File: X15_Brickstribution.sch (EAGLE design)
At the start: 42 parts, among them Q1 310mA/60V/1.6Ω

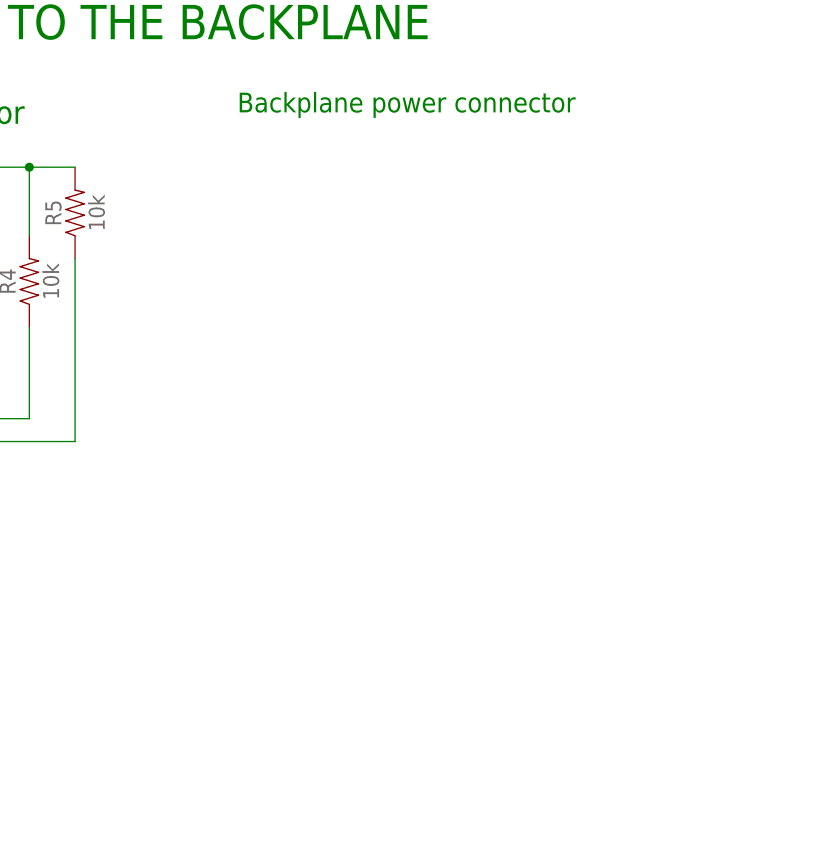
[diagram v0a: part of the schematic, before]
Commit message: Schematic V1 - Added Backplane Connections
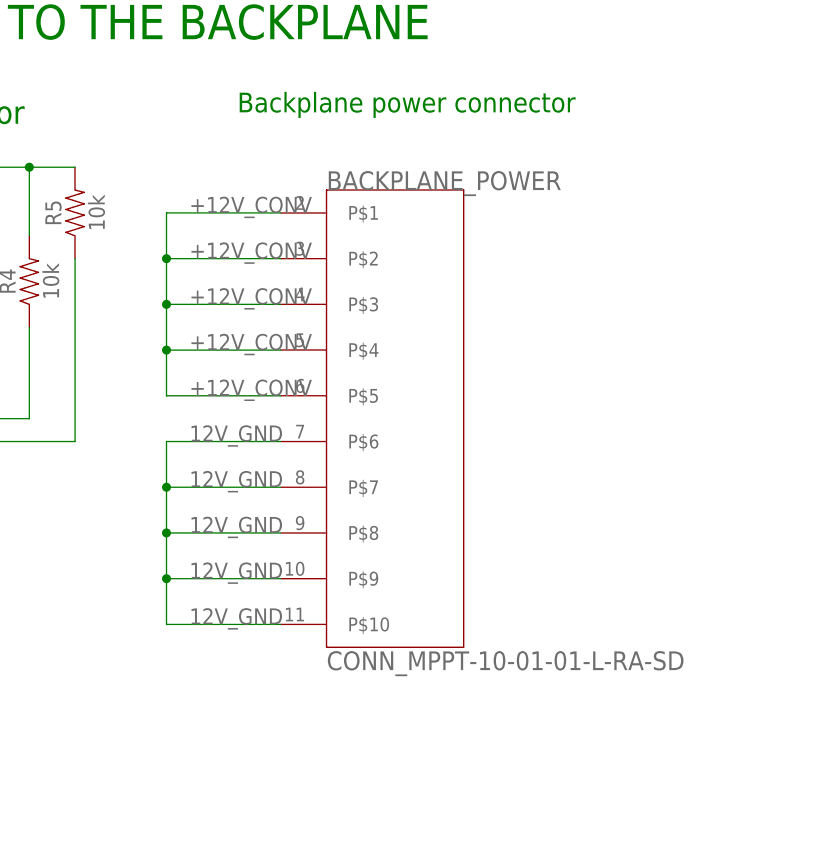
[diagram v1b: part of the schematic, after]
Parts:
- added BACKPLANE_POWER: CONN_MPPT-10-01-01-L-RA-SD, X15_Brickstribution:CONN_MPPT-10-01-01-L-RA-SD
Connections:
- net +12V_CONV: now also BACKPLANE_POWER.P$1, BACKPLANE_POWER.P$2, BACKPLANE_POWER.P$3, BACKPLANE_POWER.P$4, BACKPLANE_POWER.P$5
- net 12V_GND: now also BACKPLANE_POWER.P$10, BACKPLANE_POWER.P$6, BACKPLANE_POWER.P$7, BACKPLANE_POWER.P$8, BACKPLANE_POWER.P$9
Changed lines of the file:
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@@
 <part name="D10" library="SparkFun-LED" library_urn="urn:adsk.eagle:library:529" deviceset="LED-BLUE" device="0603" package3d_urn="urn:adsk.eagle:package:39354/1" value="BLUE"/>
 <part name="D11" library="SparkFun-LED" library_urn="urn:adsk.eagle:library:529" deviceset="LED-WHITE" device="0603" package3d_urn="urn:adsk.eagle:package:39354/1" value="WHITE"/>
+<part name="BACKPLANE_POWER" library="X15_Brickstribution" deviceset="CONN_MPPT-10-01-01-L-RA-SD" device=""/>
 </parts>
 <sheets>
@@
 <attribute name="VALUE" x="334.772" y="78.105" size="1.778" layer="96" font="vector" rot="R180" align="top-left"/>
 </instance>
+<instance part="BACKPLANE_POWER" gate="A" x="355.6" y="180.34" smashed="yes">
+<attribute name="NAME" x="347.98" y="205.74" size="2.0828" layer="95" ratio="6"/>
+<attribute name="VALUE" x="347.98" y="152.4" size="2.0828" layer="95" ratio="6"/>
+</instance>
 </instances>
 <busses>
@@
 <label x="345.44" y="101.6" size="1.778" layer="95" align="bottom-right"/>
 </segment>
+<segment>
+<pinref part="BACKPLANE_POWER" gate="A" pin="P$6"/>
+<wire x1="342.9" y1="177.8" x2="330.2" y2="177.8" width="0.1524" layer="91"/>
+<label x="332.74" y="177.8" size="1.778" layer="95"/>
+<wire x1="330.2" y1="177.8" x2="330.2" y2="172.72" width="0.1524" layer="91"/>
+<pinref part="BACKPLANE_POWER" gate="A" pin="P$8"/>
+<wire x1="330.2" y1="172.72" x2="330.2" y2="167.64" width="0.1524" layer="91"/>
+<wire x1="342.9" y1="167.64" x2="330.2" y2="167.64" width="0.1524" layer="91"/>
+<label x="332.74" y="167.64" size="1.778" layer="95"/>
+<pinref part="BACKPLANE_POWER" gate="A" pin="P$7"/>
+<wire x1="342.9" y1="172.72" x2="330.2" y2="172.72" width="0.1524" layer="91"/>
+<label x="332.74" y="172.72" size="1.778" layer="95"/>
+<junction x="330.2" y="172.72"/>
+<pinref part="BACKPLANE_POWER" gate="A" pin="P$9"/>
+<wire x1="342.9" y1="162.56" x2="330.2" y2="162.56" width="0.1524" layer="91"/>
+<label x="332.74" y="162.56" size="1.778" layer="95"/>
+<wire x1="330.2" y1="167.64" x2="330.2" y2="162.56" width="0.1524" layer="91"/>
+<junction x="330.2" y="167.64"/>
+<pinref part="BACKPLANE_POWER" gate="A" pin="P$10"/>
+<wire x1="342.9" y1="157.48" x2="330.2" y2="157.48" width="0.1524" layer="91"/>
+<label x="332.74" y="157.48" size="1.778" layer="95"/>
+<wire x1="330.2" y1="162.56" x2="330.2" y2="157.48" width="0.1524" layer="91"/>
+<junction x="330.2" y="162.56"/>
+</segment>
 </net>
 <net name="+12V" class="0">
@@
 <wire x1="25.4" y1="121.92" x2="25.4" y2="119.38" width="0.1524" layer="91"/>
 </segment>
-</net>
+<segment>
+<pinref part="BACKPLANE_POWER" gate="A" pin="P$1"/>
+<wire x1="342.9" y1="203.2" x2="330.2" y2="203.2" width="0.1524" layer="91"/>
+<label x="332.74" y="203.2" size="1.778" layer="95"/>
+<pinref part="BACKPLANE_POWER" gate="A" pin="P$2"/>
+<wire x1="342.9" y1="198.12" x2="330.2" y2="198.12" width="0.1524" layer="91"/>
+<label x="332.74" y="198.12" size="1.778" layer="95"/>
+<wire x1="330.2" y1="203.2" x2="330.2" y2="198.12" width="0.1524" layer="91"/>
+<pinref part="BACKPLANE_POWER" gate="A" pin="P$3"/>
+<wire x1="342.9" y1="193.04" x2="330.2" y2="193.04" width="0.1524" layer="91"/>
+<label x="332.74" y="193.04" size="1.778" layer="95"/>
+<wire x1="330.2" y1="198.12" x2="330.2" y2="193.04" width="0.1524" layer="91"/>
+<junction x="330.2" y="198.12"/>
+<pinref part="BACKPLANE_POWER" gate="A" pin="P$4"/>
+<wire x1="342.9" y1="187.96" x2="330.2" y2="187.96" width="0.1524" layer="91"/>
+<label x="332.74" y="187.96" size="1.778" layer="95"/>
+<wire x1="330.2" y1="193.04" x2="330.2" y2="187.96" width="0.1524" layer="91"/>
+<junction x="330.2" y="193.04"/>
+<pinref part="BACKPLANE_POWER" gate="A" pin="P$5"/>
+<wire x1="342.9" y1="182.88" x2="330.2" y2="182.88" width="0.1524" layer="91"/>
+<label x="332.74" y="182.88" size="1.778" layer="95"/>
+<wire x1="330.2" y1="187.96" x2="330.2" y2="182.88" width="0.1524" layer="91"/>
+<junction x="330.2" y="187.96"/>
+</segment>
+</net>

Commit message: Schematic Revision V1
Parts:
- added C10, C17, C18, C19, C8, C9: 2.2uF, SparkFun-Capacitors:2.2UF-0603-10V-20%
- added C11, C20: 1000uF, X15_Brickstribution:CAP_PCG1A102MCL1GSCAP_PC_10X12P7_NCH-M
- added C12, C21: 1.0uF, SparkFun-Capacitors:1.0UF-0603-16V-10%
- added C13, C4: 0.22uF, SparkFun-Capacitors:0.22UF-0603-25V-10%
- added C14, C5: 2.2nF, SparkFun-Capacitors:2.2NF/2200PF-0603-50V-10%
- added C15, C6: 390pF, SparkFun-Capacitors:390NF-0603-10V-10%
- added C16, C7: 22nF, SparkFun-Capacitors:22NF/22,000PF-0603-50V-10%
- added R12, R16: 15k, SparkFun-Resistors:15KOHM-0603-1/10W-1%
- added R13, R17: 16k, SparkFun-Resistors:16.2KOHM-0603-1/10W-1%
- added R14, R18: 10k, SparkFun-Resistors:10KOHM-0603-1/10W-1%
- added R15, R19: 20k, SparkFun-Resistors:20KOHM-0603-1/10W-1%
- added R20: DIODE_RBQ30NS45AFHTLTRANS_R5009FNJ_ROM-M, X15_Brickstribution:DIODE_RBQ30NS45AFHTLTRANS_R5009FNJ_ROM-M
- added U$2, U$3: 40uH, X15_Brickstribution:IND_PG1096_26X26_PUL-M
- added U$4: CONN_MPPT-10-01-01-L-RA-SD, X15_Brickstribution:CONN_MPPT-10-01-01-L-RA-SD
- added U1, U2: IC_L4970A, X15_Brickstribution:IC_L4970A
- added U3, U4: DIODE_STPS1545CT, X15_Brickstribution:DIODE_STPS1545CT
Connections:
- new net +7.4V_SERVO: R20.2, U$4.P$1, U$4.P$2, U$4.P$3, U$4.P$4, U$4.P$5
- new net N$11: C7.1, R12.2
- new net N$14: C13.1, C4.1, U1.BOOT, U2.BOOT
- new net N$15: C14.2, C5.2, U1.C_OSC, U2.C_OSC
- new net N$16: C15.2, C16.2, C6.2, C7.2, U1.FCOMP, U2.FCOMP
- new net N$17: R13.2, R17.2, U1.R_OSC, U2.R_OSC
- new net N$18: C17.2, C8.2, U1.SS, U2.SS
- new net N$20: C18.2, C9.2, U1.VREF, U2.VREF
- new net N$22: C13.2, C4.2, U$2.2, U$3.2, U1.OUT, U2.OUT, U3.2, U4.2
- new net N$24: C10.2, C19.2, U1.VSTART, U2.VSTART
- new net N$3: C16.1, R16.2
- new net NC: U1.RST_DLY, U1.RST_OUT, U1.SYNC, U2.RST_DLY, U2.RST_OUT, U2.SYNC
- new net VOUT1: C11.1, C12.2, R14.2, R20.3, U$2.1
- new net VOUT2: C20.1, C21.2, R18.2, R20.1, U$3.1
- new net VREF1: R14.1, R15.2, U1.FB
- new net VREF2: R18.1, R19.2, U2.FB
- net +12V_CONV: now also U1.VI, U2.VI
- net 12V_GND: now also C10.1, C11.2, C12.1, C14.1, C15.1, C17.1, C18.1, C19.1, C20.2, C21.1, C5.1, C6.1, C8.1, C9.1, R12.1, R13.1, R15.1, R16.1, R17.1, R19.1, U$4.P$10, U$4.P$6, U$4.P$7, U$4.P$8, U$4.P$9, U1.GND, U1.RST, U2.GND, U2.RST, U3.1, U3.3, U4.1, U4.3
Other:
- note added: "CONNECTIONS TO SERVOS"

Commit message: Cleaned all backup files and updated schematic for revisions v1
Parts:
- removed BRICK: BMR480_CONNECTOR, X15_Brickstribution:BMR480_CONNECTOR
- removed C10, C17, C18, C19, C8, C9: 2.2uF, SparkFun-Capacitors:2.2UF-0603-10V-20%
- removed C11, C20: 1000uF, X15_Brickstribution:CAP_PCG1A102MCL1GSCAP_PC_10X12P7_NCH-M
- removed C12, C21: 1.0uF, SparkFun-Capacitors:1.0UF-0603-16V-10%
- removed C13, C4: 0.22uF, SparkFun-Capacitors:0.22UF-0603-25V-10%
- removed C14, C5: 2.2nF, SparkFun-Capacitors:2.2NF/2200PF-0603-50V-10%
- removed C15, C6: 390pF, SparkFun-Capacitors:390NF-0603-10V-10%
- removed C16, C7: 22nF, SparkFun-Capacitors:22NF/22,000PF-0603-50V-10%
- removed R12, R16: 15k, SparkFun-Resistors:15KOHM-0603-1/10W-1%
- removed R13, R17: 16k, SparkFun-Resistors:16.2KOHM-0603-1/10W-1%
- removed R14, R18: 10k, SparkFun-Resistors:10KOHM-0603-1/10W-1%
- removed R15, R19: 20k, SparkFun-Resistors:20KOHM-0603-1/10W-1%
- removed R20: DIODE_RBQ30NS45AFHTLTRANS_R5009FNJ_ROM-M, X15_Brickstribution:DIODE_RBQ30NS45AFHTLTRANS_R5009FNJ_ROM-M
- removed U$3: 40uH, X15_Brickstribution:IND_PG1096_26X26_PUL-M
- removed U$4: CONN_MPPT-10-01-01-L-RA-SD, X15_Brickstribution:CONN_MPPT-10-01-01-L-RA-SD
- removed U1, U2: IC_L4970A, X15_Brickstribution:IC_L4970A
- removed U3, U4: DIODE_STPS1545CT, X15_Brickstribution:DIODE_STPS1545CT
- added +7.4VOUT1_TEST, +7.4VOUT2_TEST, +7.4V_SERVO_TEST, 7.4V_GND: (no value), SparkFun-Connectors:CONN_01
- added C22, C31: 0.22uF, SparkFun-Capacitors:0.22UF-0603-25V-10%
- added C23, C32: 2.2nF, SparkFun-Capacitors:2.2NF/2200PF-0603-50V-10%
- added C24, C33: 390pF, SparkFun-Capacitors:390NF-0603-10V-10%
- added C25, C34: 22nF, SparkFun-Capacitors:22NF/22,000PF-0603-50V-10%
- added C26, C27, C28, C35, C36, C37: 2.2uF, SparkFun-Capacitors:2.2UF-0603-10V-20%
- added C29, C38: 1000uF, X15_Brickstribution:CAP_PCG1A102MCL1GSCAP_PC_10X12P7_NCH-M
- added C30, C39: 1.0uF, SparkFun-Capacitors:1.0UF-0603-16V-10%
- added D12, D13: GREEN, SparkFun-LED:LED-GREEN0603
- added R21, R22: 470, SparkFun-Resistors:470OHM-0603-1/10W-1%
- added R23, R27: 15k, SparkFun-Resistors:15KOHM-0603-1/10W-1%
- added R24, R28: 16k, SparkFun-Resistors:16.2KOHM-0603-1/10W-1%
- added R25, R29: 10k, SparkFun-Resistors:10KOHM-0603-1/10W-1%
- added R26, R30: 20k, SparkFun-Resistors:20KOHM-0603-1/10W-1%
- added R31: DIODE_RBQ30NS45AFHTLTRANS_R5009FNJ_ROM-M, X15_Brickstribution:DIODE_RBQ30NS45AFHTLTRANS_R5009FNJ_ROM-M
- added U$5, U$6: 40uH, X15_Brickstribution:IND_PG1096_26X26_PUL-M
- added U$7: CONN_MPPT-10-01-01-L-RA-SD, X15_Brickstribution:CONN_MPPT-10-01-01-L-RA-SD
- added U5, U7: IC_L4970A, X15_Brickstribution:IC_L4970A
- added U6, U8: DIODE_STPS1545CT, X15_Brickstribution:DIODE_STPS1545CT
- U$2: value 40uH -> CONN_BMR480_CONNECTOR; device X15_Brickstribution:IND_PG1096_26X26_PUL-M -> X15_Brickstribution:CONN_BMR480_CONNECTOR
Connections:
- removed net N$11: C7.1, R12.2
- removed net N$16: C15.2, C16.2, C6.2, C7.2, U1.FCOMP, U2.FCOMP
- removed net N$17: R13.2, R17.2, U1.R_OSC, U2.R_OSC
- removed net N$18: C17.2, C8.2, U1.SS, U2.SS
- removed net N$20: C18.2, C9.2, U1.VREF, U2.VREF
- removed net N$22: C13.2, C4.2, U$2.2, U$3.2, U1.OUT, U2.OUT, U3.2, U4.2
- removed net N$24: C10.2, C19.2, U1.VSTART, U2.VSTART
- new net BOOT2: C31.1, U7.BOOT
- new net BOOT_1: C22.1, U5.BOOT
- new net C_OSC1: C23.2, U5.C_OSC
- new net C_OSC2: C32.2, U7.C_OSC
- new net FCOMP1: C24.2, C25.2, U5.FCOMP
- new net FCOMP2: C33.2, C34.2, U7.FCOMP
- new net N$12: D12.A, R21.2
- new net N$13: D13.A, R22.2
- new net OUT1: C22.2, U$5.2, U5.OUT, U6.2
- new net OUT2: C31.2, U$6.2, U7.OUT, U8.2
- new net R_OSC1: R24.2, U5.R_OSC
- new net R_OSC2: R28.2, U7.R_OSC
- new net SS1: C26.2, U5.SS
- new net SS2: C35.2, U7.SS
- new net VSTART1: C28.2, U5.VSTART
- new net VSTART2: C37.2, U7.VSTART
- new net V_REF_CAP1: C27.2, U5.VREF
- new net V_REF_CAP2: C36.2, U7.VREF
- net +12V: now also R22.1, U$2.+12V0; no longer BRICK.+12V0, BRICK.+12V1
- net +12V_CONV: now also BACKPLANE_POWER.VDD1, BACKPLANE_POWER.VDD2, BACKPLANE_POWER.VDD3, BACKPLANE_POWER.VDD4, BACKPLANE_POWER.VDD5, U5.VI, U7.VI; no longer BACKPLANE_POWER.P$1, BACKPLANE_POWER.P$2, BACKPLANE_POWER.P$3, BACKPLANE_POWER.P$4, BACKPLANE_POWER.P$5, U1.VI, U2.VI
- net +48V: now also U$2.+48V; no longer BRICK.+48V
- net +7.4V_SERVO: now also +7.4V_SERVO_TEST.1, R31.2, U$7.VDD1, U$7.VDD2, U$7.VDD3, U$7.VDD4, U$7.VDD5; no longer R20.2, U$4.P$1, U$4.P$2, U$4.P$3, U$4.P$4, U$4.P$5
- net 12V_GND: now also BACKPLANE_POWER.GND1, BACKPLANE_POWER.GND2, BACKPLANE_POWER.GND3, BACKPLANE_POWER.GND4, BACKPLANE_POWER.GND5, C23.1, C24.1, C26.1, C27.1, C28.1, C29.2, C30.1, C32.1, C33.1, C35.1, C36.1, C37.1, C38.2, C39.1, D12.C, D13.C, R23.1, R24.1, R26.1, R27.1, R28.1, R30.1, U$2.12V_GND0, U$7.GND1, U$7.GND2, U$7.GND3, U$7.GND4, U$7.GND5, U5.GND, U5.RST, U6.1, U6.3, U7.GND, U7.RST, U8.1, U8.3; no longer BACKPLANE_POWER.P$10, BACKPLANE_POWER.P$6, BACKPLANE_POWER.P$7, BACKPLANE_POWER.P$8, BACKPLANE_POWER.P$9, BRICK.12V_GND0, BRICK.12V_GND1, C10.1, C11.2, C12.1, C14.1, C15.1, C17.1, C18.1, C19.1, C20.2, C21.1, C5.1, C6.1, C8.1, C9.1, R12.1, R13.1, R15.1, R16.1, R17.1, R19.1, U$4.P$10, U$4.P$6, U$4.P$7, U$4.P$8, U$4.P$9, U1.GND, U1.RST, U2.GND, U2.RST, U3.1, U3.3, U4.1, U4.3
- net 48V_GND: now also U$2.48V_GND; no longer BRICK.48V_GND
- net D_GND: now also 7.4V_GND.1
- net N$14: now also C25.1, R23.2; no longer C13.1, C4.1, U1.BOOT, U2.BOOT
- net N$15: now also C34.1, R27.2; no longer C14.2, C5.2, U1.C_OSC, U2.C_OSC
- net N$2: now also U$2.12V_GND1; no longer BRICK.RMCONT
- net N$3: now also U$2.+12V1; no longer C16.1, R16.2
- net NC: now also U$2.RMCONT, U5.RST_DLY, U5.RST_OUT, U5.SYNC, U7.RST_DLY, U7.RST_OUT, U7.SYNC; no longer U1.RST_DLY, U1.RST_OUT, U1.SYNC, U2.RST_DLY, U2.RST_OUT, U2.SYNC
- net VOUT1: now also +7.4VOUT1_TEST.1, C29.1, C30.2, R21.1, R25.2, R31.3, U$5.1; no longer C11.1, C12.2, R14.2, R20.3, U$2.1
- net VOUT2: now also +7.4VOUT2_TEST.1, C38.1, C39.2, R29.2, R31.1, U$6.1; no longer C20.1, C21.2, R18.2, R20.1, U$3.1
- net VREF1: now also R25.1, R26.2, U5.FB; no longer R14.1, R15.2, U1.FB
- net VREF2: now also R29.1, R30.2, U7.FB; no longer R18.1, R19.2, U2.FB
